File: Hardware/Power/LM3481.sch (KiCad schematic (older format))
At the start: 22 parts, among them IC1 LM3481MM, Q1 2N7000, Q2 AO4264E

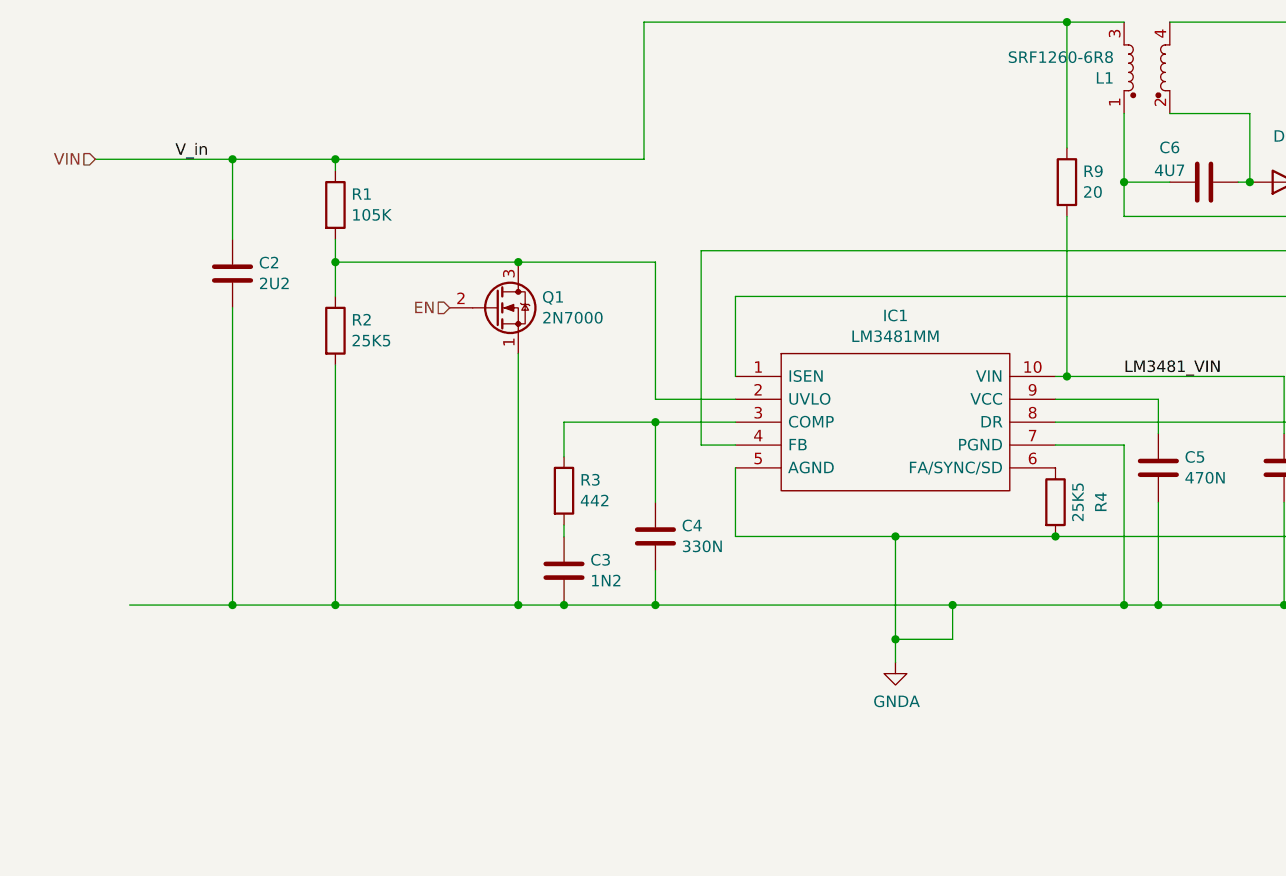
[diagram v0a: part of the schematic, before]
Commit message: Moved MCU Power Supply to Logic Board
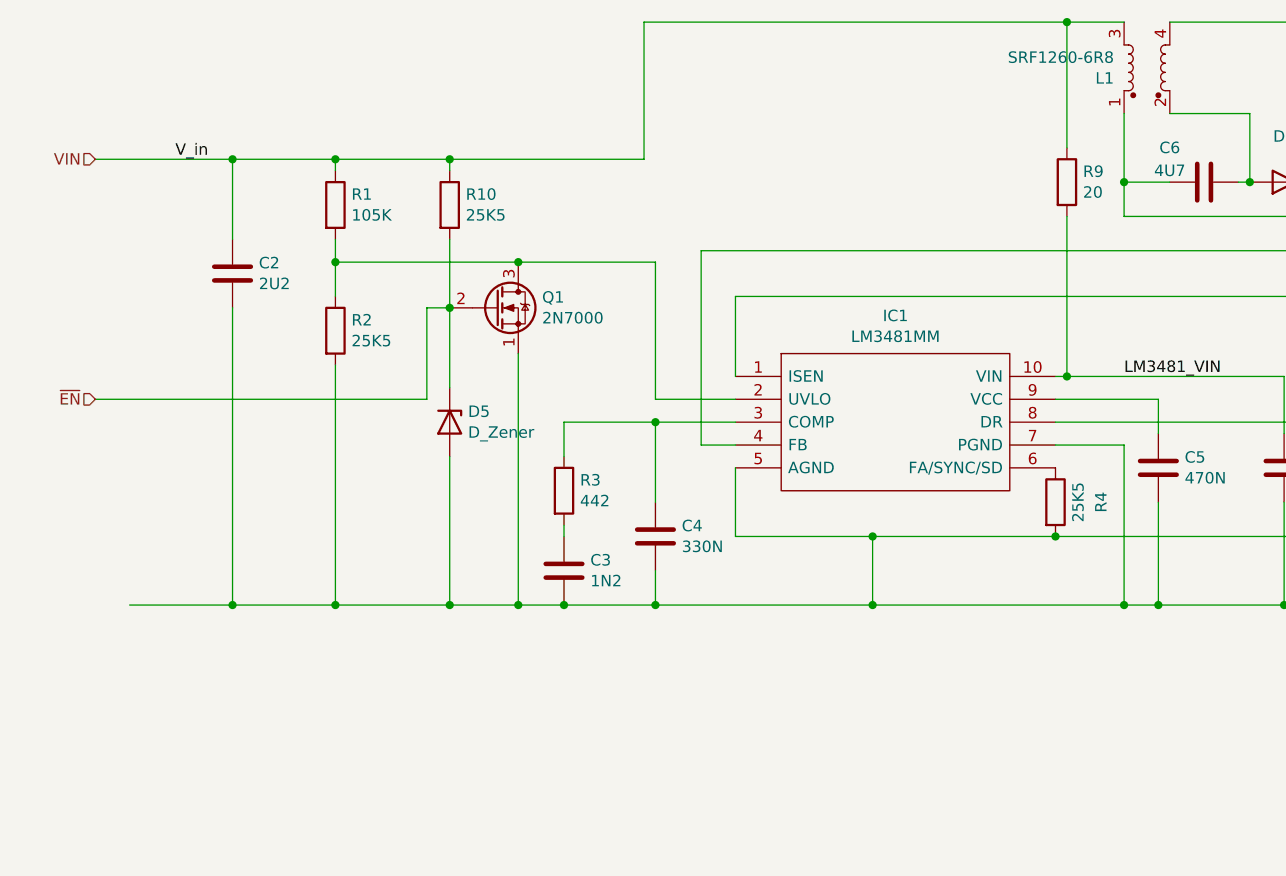
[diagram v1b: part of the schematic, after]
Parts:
- added D5: D_Zener, Diode_SMD:D_SOD-323_HandSoldering, symbol Device:D_Zener
- added R10: 25K5, Resistor_SMD:R_0603_1608Metric_Pad1.05x0.95mm_HandSolder, symbol Device:R
- D1: Arrow Part Number (none) -> C19229; Mouser Part Number C19229 -> (none)
- IC1: Manufacturer_Part_Number LM3481MM -> (none); Mouser Part Number (none) -> LM3481MM
- L1: Manufacturer_Part_Number SRF1260-6R8 -> (none); Mouser Part Number (none) -> SRF1260-6R8
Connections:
- net VIN: now also R10.1
- net EN renamed ~EN
- net ~EN: now also D5.1 (K), R10.2
- net GNDA renamed GNDPWR
- net GNDPWR: now also D5.2 (A)
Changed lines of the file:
@@
 F 2 "ArduinoLamp:D_SMC_Handsoldering_Shortened" H 7250 2900 50  0001 C CNN
 F 3 "~" H 7250 2900 50  0001 C CNN
-F 4 "C19229" H 7250 2900 50  0001 C CNN "Mouser Part Number"
+F 4 "" H 7250 2900 50  0001 C CNN "Mouser Part Number"
+F 5 "C19229" H 7250 2900 50  0001 C CNN "Arrow Part Number"
 	1    7250 2900
 	-1   0    0    1
@@
 F 2 "ArduinoLamp:L_Bourns_SRF1260_HandSoldering" H 6650 2400 50  0001 C CNN
 F 3 "~" H 6650 2400 50  0001 C CNN
-F 4 "SRF1260-6R8" H 6650 2400 50  0001 C CNN "Manufacturer_Part_Number"
+F 4 "" H 6650 2400 50  0001 C CNN "Manufacturer_Part_Number"
+F 5 "SRF1260-6R8" H 6650 2400 50  0001 C CNN "Mouser Part Number"
 	1    6650 2400
 	0    -1   -1   0
@@
 F 5 "1.1" H 6100 3550 50  0001 L CNN "Height"
 F 6 "Texas Instruments" H 6100 3450 50  0001 L CNN "Manufacturer_Name"
-F 7 "LM3481MM" H 6100 3350 50  0001 L CNN "Manufacturer_Part_Number"
+F 7 "" H 6100 3350 50  0001 L CNN "Manufacturer_Part_Number"
 F 8 "" H 6100 3250 50  0001 L CNN "Arrow Part Number"
 F 9 "" H 6100 3150 50  0001 L CNN "Arrow Price/Stock"
-F 10 "" H 6100 3050 50  0001 L CNN "Mouser Part Number"
+F 10 "LM3481MM" H 6100 3050 50  0001 L CNN "Mouser Part Number"
 F 11 "" H 6100 2950 50  0001 L CNN "Mouser Price/Stock"
 	1    4850 3750
@@
 V_in
 Wire Wire Line
-	3100 2800 4450 2800
+	3100 2800 3600 2800
+Text HLabel 2050 2800 0    50   Input ~ 0
+VIN
+Text HLabel 10150 3350 2    50   Input ~ 0
+VOUT
+Connection ~ 4100 4750
+Wire Wire Line
+	4100 4750 3900 4750
+Wire Wire Line
+	4100 4750 4500 4750
+Wire Wire Line
+	4500 4300 4500 3950
+Connection ~ 4500 3950
+Wire Wire Line
+	4500 3950 4850 3950
+Wire Wire Line
+	4500 4600 4500 4750
+Connection ~ 4500 4750
+Wire Wire Line
+	4100 4100 4100 3950
+Wire Wire Line
+	4100 3950 4500 3950
+Wire Wire Line
+	4100 4400 4100 4450
+Text Notes 7350 7500 0    50   ~ 0
+LM3481 SEPIC Converter
+Connection ~ 3900 4750
+Wire Wire Line
+	3900 3650 3900 4750
+Wire Wire Line
+	2200 4750 2650 4750
+Connection ~ 2650 4750
+Wire Wire Line
+	2650 4750 3100 4750
+Connection ~ 3100 4750
+Wire Wire Line
+	3100 4750 3600 4750
+Wire Wire Line
+	6750 2200 8800 2200
+Wire Wire Line
+	8800 2200 8800 4750
+Connection ~ 8800 4750
+Wire Wire Line
+	8800 4750 9150 4750
+Wire Wire Line
+	9600 3350 10150 3350
+Wire Wire Line
+	2050 2800 2650 2800
+Text Label 6550 3750 0    50   ~ 0
+LM3481_VIN
+Connection ~ 7250 4750
+Wire Wire Line
+	6250 4050 6550 4050
+Wire Wire Line
+	6550 4050 6550 4750
+Connection ~ 6550 4750
+Wire Wire Line
+	6550 4750 6700 4750
+Wire Wire Line
+	6700 4300 6700 4750
+Connection ~ 6700 4750
+Wire Wire Line
+	6700 4750 7250 4750
+Wire Wire Line
+	4850 4150 4850 4450
+Wire Wire Line
+	7750 4750 8400 4750
+Wire Wire Line
+	8400 4000 8400 4050
+Connection ~ 8400 4000
+Wire Wire Line
+	8400 4350 8400 4750
+Connection ~ 8400 4750
+Wire Wire Line
+	8400 4750 8800 4750
+Wire Wire Line
+	6250 4450 9150 4450
+Wire Wire Line
+	9150 4450 9150 4150
+Connection ~ 6250 4450
+Wire Wire Line
+	4450 2200 6300 2200
+$Comp
+L Device:R R9
+U 1 1 5FA1346B
+P 6300 2900
+F 0 "R9" H 6370 2946 50  0000 L CNN
+F 1 "20" H 6370 2855 50  0000 L CNN
+F 2 "Resistor_SMD:R_0603_1608Metric_Pad1.05x0.95mm_HandSolder" V 6230 2900 50  0001 C CNN
+F 3 "~" H 6300 2900 50  0001 C CNN
+F 4 "RS-03K19R6FT" H 6300 2900 50  0001 C CNN "Manufacturer_Part_Number"
+	1    6300 2900
+	1    0    0    -1
+$EndComp
+Wire Wire Line
+	6300 2750 6300 2200
+Connection ~ 6300 2200
+Wire Wire Line
+	6300 2200 6550 2200
+Wire Wire Line
+	6300 3050 6300 3750
+Wire Wire Line
+	6250 3750 6300 3750
+Connection ~ 6300 3750
+Wire Wire Line
+	6300 3750 7250 3750
+Wire Wire Line
+	4850 4450 5450 4450
+Wire Wire Line
+	4500 4750 5450 4750
+Wire Wire Line
+	3900 3250 4500 3250
+Connection ~ 3900 3250
 Wire Wire Line
 	3100 3250 3900 3250
@@
 	1    0    0    -1
 $EndComp
-Connection ~ 3900 3250
-Wire Wire Line
-	3900 3250 4500 3250
-Text HLabel 2050 2800 0    50   Input ~ 0
-VIN
-Text HLabel 3600 3450 0    50   Input ~ 0
-EN
-Text HLabel 10150 3350 2    50   Input ~ 0
-VOUT
-Connection ~ 4100 4750
-Wire Wire Line
-	4100 4750 3900 4750
-Wire Wire Line
-	4100 4750 4500 4750
-Wire Wire Line
-	4500 4300 4500 3950
-Connection ~ 4500 3950
-Wire Wire Line
-	4500 3950 4850 3950
-Wire Wire Line
-	4500 4600 4500 4750
-Connection ~ 4500 4750
-Wire Wire Line
-	4100 4100 4100 3950
-Wire Wire Line
-	4100 3950 4500 3950
-Wire Wire Line
-	4100 4400 4100 4450
-Text Notes 7350 7500 0    50   ~ 0
-LM3481 SEPIC Converter
-Connection ~ 3900 4750
-Wire Wire Line
-	3900 3650 3900 4750
-Wire Wire Line
-	2200 4750 2650 4750
-Connection ~ 2650 4750
-Wire Wire Line
-	2650 4750 3100 4750
-Connection ~ 3100 4750
-Wire Wire Line
-	3100 4750 3900 4750
-Wire Wire Line
-	6750 2200 8800 2200
-Wire Wire Line
-	8800 2200 8800 4750
-Connection ~ 8800 4750
-Wire Wire Line
-	8800 4750 9150 4750
-Wire Wire Line
-	9600 3350 10150 3350
-Wire Wire Line
-	2050 2800 2650 2800
-Text Label 6550 3750 0    50   ~ 0
-LM3481_VIN
-$Comp
-L power:GNDA #PWR0113
-U 1 1 5F9A8242
-P 5550 5000
-F 0 "#PWR0113" H 5550 4750 50  0001 C CNN
-F 1 "GNDA" H 5555 4827 50  0000 C CNN
-F 2 "" H 5550 5000 50  0001 C CNN
-F 3 "" H 5550 5000 50  0001 C CNN
-	1    5550 5000
-	1    0    0    -1
-$EndComp
-Connection ~ 7250 4750
-Wire Wire Line
-	6250 4050 6550 4050
-Wire Wire Line
-	6550 4050 6550 4750
-Connection ~ 6550 4750
-Wire Wire Line
-	6550 4750 6700 4750
-Wire Wire Line
-	6700 4300 6700 4750
-Connection ~ 6700 4750
-Wire Wire Line
-	6700 4750 7250 4750
-Wire Wire Line
-	4500 4750 5800 4750
-Wire Wire Line
-	4850 4150 4850 4450
-Wire Wire Line
-	4850 4450 5550 4450
-Wire Wire Line
-	5550 4450 5550 4900
-Connection ~ 5550 4450
-Wire Wire Line
-	5550 4450 6250 4450
-Wire Wire Line
-	7750 4750 8400 4750
-Wire Wire Line
-	8400 4000 8400 4050
-Connection ~ 8400 4000
-Wire Wire Line
-	8400 4350 8400 4750
-Connection ~ 8400 4750
-Wire Wire Line
-	8400 4750 8800 4750
-Wire Wire Line
-	6250 4450 9150 4450
-Wire Wire Line
-	9150 4450 9150 4150
-Connection ~ 6250 4450
-Wire Wire Line
-	5550 4900 5800 4900
-Wire Wire Line
-	5800 4900 5800 4750
-Connection ~ 5550 4900
-Wire Wire Line
-	5550 4900 5550 5000
-Connection ~ 5800 4750
-Wire Wire Line
-	5800 4750 6550 4750
-Wire Wire Line
-	4450 2200 6300 2200
-$Comp
-L Device:R R9
-U 1 1 5FA1346B
-P 6300 2900
-F 0 "R9" H 6370 2946 50  0000 L CNN
-F 1 "20" H 6370 2855 50  0000 L CNN
-F 2 "Resistor_SMD:R_0603_1608Metric_Pad1.05x0.95mm_HandSolder" V 6230 2900 50  0001 C CNN
-F 3 "~" H 6300 2900 50  0001 C CNN
-F 4 "RS-03K19R6FT" H 6300 2900 50  0001 C CNN "Manufacturer_Part_Number"
-	1    6300 2900
-	1    0    0    -1
-$EndComp
-Wire Wire Line
-	6300 2750 6300 2200
-Connection ~ 6300 2200
-Wire Wire Line
-	6300 2200 6550 2200
-Wire Wire Line
-	6300 3050 6300 3750
-Wire Wire Line
-	6250 3750 6300 3750
-Connection ~ 6300 3750
-Wire Wire Line
-	6300 3750 7250 3750
+$Comp
+L Device:R R10
+U 1 1 5FBCFFB7
+P 3600 3000
+F 0 "R10" H 3670 3046 50  0000 L CNN
+F 1 "25K5" H 3670 2955 50  0000 L CNN
+F 2 "Resistor_SMD:R_0603_1608Metric_Pad1.05x0.95mm_HandSolder" V 3530 3000 50  0001 C CNN
+F 3 "~" H 3600 3000 50  0001 C CNN
+F 4 "RS-05K2552FT" H 3600 3000 50  0001 C CNN "Manufacturer_Part_Number"
+	1    3600 3000
+	1    0    0    -1
+$EndComp
+Wire Wire Line
+	3600 2850 3600 2800
+Connection ~ 3600 2800
+Wire Wire Line
+	3600 2800 4450 2800
+Wire Wire Line
+	3600 3150 3600 3450
+$Comp
+L Device:D_Zener D5
+U 1 1 5FBD5B24
+P 3600 3950
+F 0 "D5" V 3554 4030 50  0000 L CNN
+F 1 "D_Zener" V 3645 4030 50  0000 L CNN
+F 2 "Diode_SMD:D_SOD-323_HandSoldering" H 3600 3950 50  0001 C CNN
+F 3 "~" H 3600 3950 50  0001 C CNN
+F 4 "MM3Z4V7ST1G" H 3600 3950 50  0001 C CNN "Mouser Part Number"
+	1    3600 3950
+	0    1    1    0
+$EndComp
+Wire Wire Line
+	3600 3450 3600 3800
+Connection ~ 3600 3450
+Wire Wire Line
+	3600 4100 3600 4750
+Connection ~ 3600 4750
+Wire Wire Line
+	3600 4750 3900 4750
+Text HLabel 2050 3850 0    50   Input ~ 0
+~EN
+Wire Wire Line
+	2050 3850 3500 3850
+Wire Wire Line
+	3500 3850 3500 3450
+Wire Wire Line
+	3500 3450 3600 3450
+Wire Wire Line
+	5450 4450 5450 4750
+Connection ~ 5450 4450
+Wire Wire Line
+	5450 4450 6250 4450
+Connection ~ 5450 4750
+Wire Wire Line
+	5450 4750 6550 4750
 $EndSCHEMATC

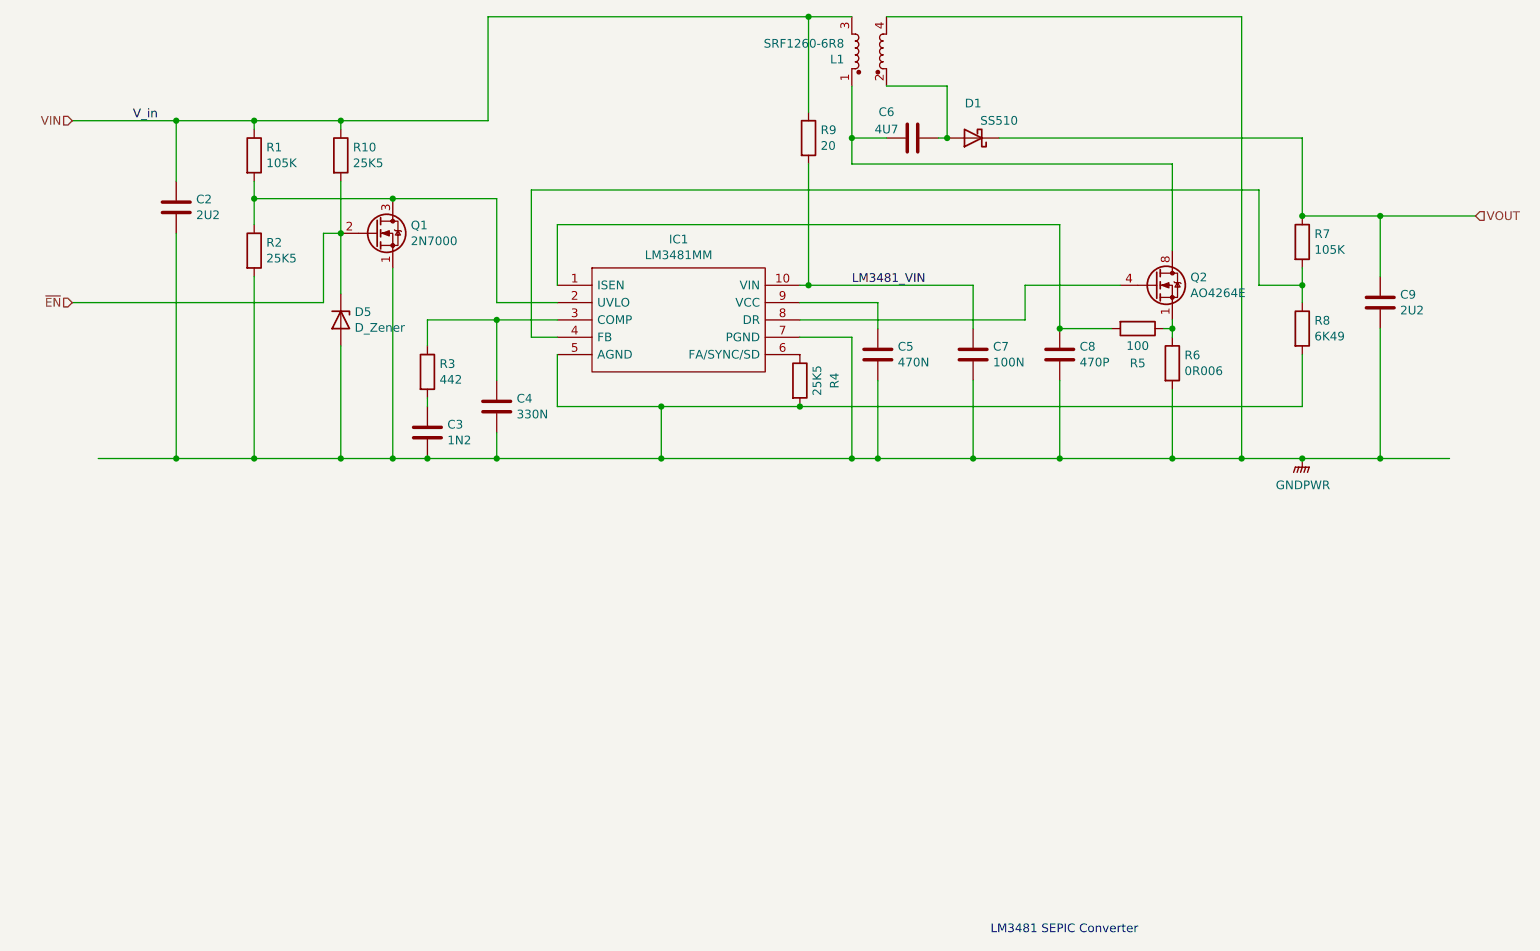
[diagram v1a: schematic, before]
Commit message: Removed Logic Board PSU from Power Board
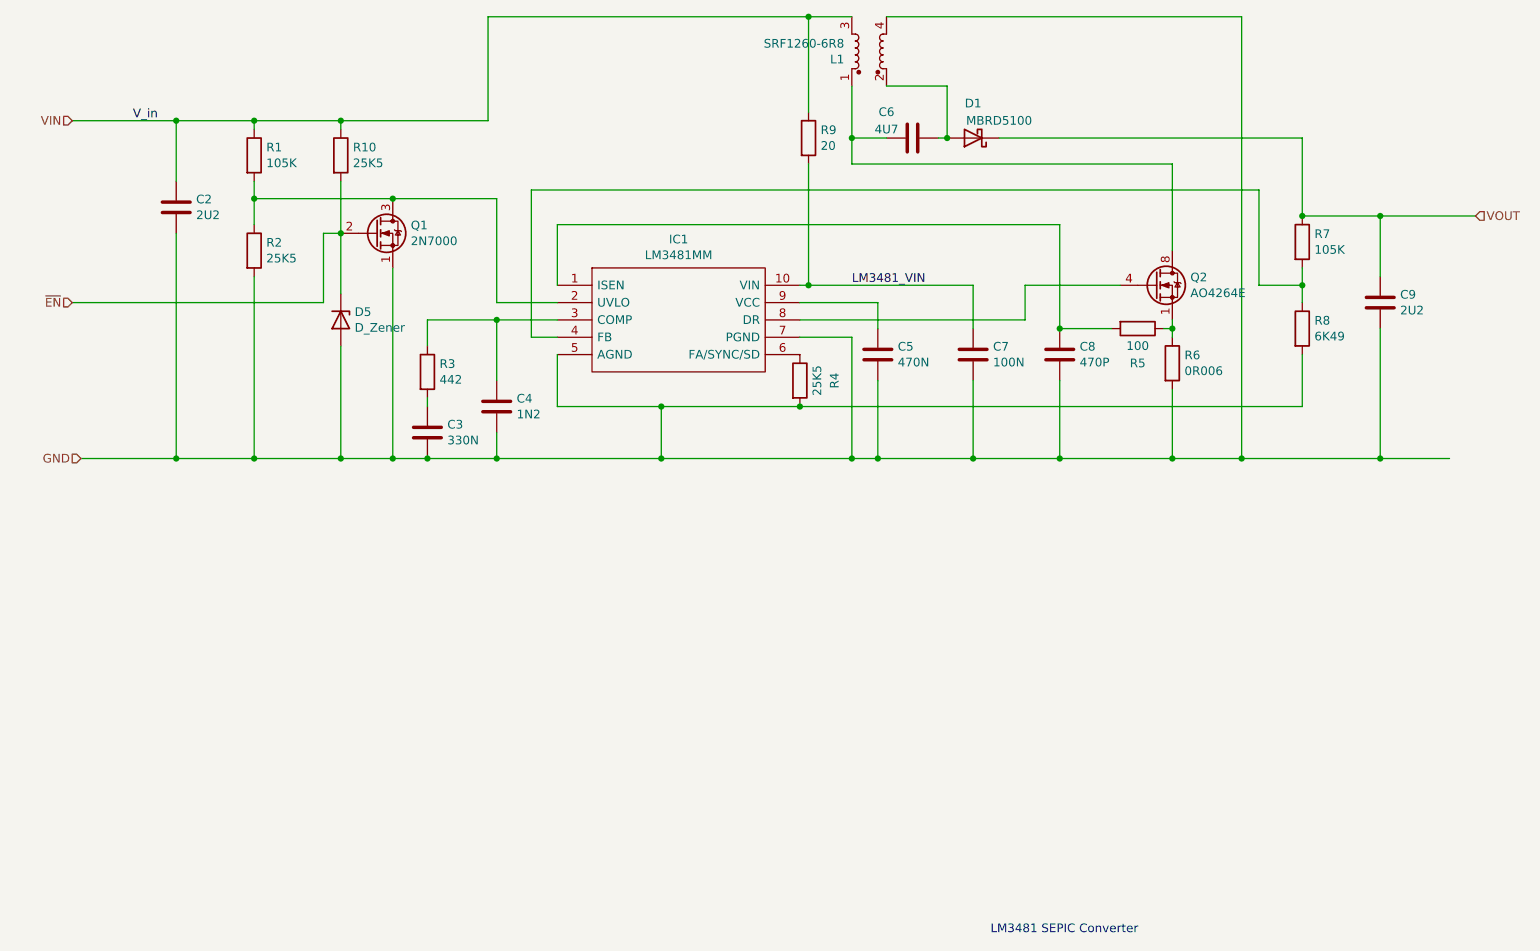
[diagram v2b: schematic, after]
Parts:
- C3: value 1N2 -> 330N; Manufacturer_Part_Number C1608C0G1H122JT000N -> TCC0603X7R334K500CT
- C4: value 330N -> 1N2; Manufacturer_Part_Number TCC0603X7R334K500CT -> C1608C0G1H122JT000N
- D1: value SS510 -> MBRD5100; footprint ArduinoLamp:D_SMC_Handsoldering_Shortened -> ArduinoLamp:TO-252-2_ConnectedPins
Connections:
- net GNDPWR renamed GND
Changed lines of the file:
@@
-	1    0    0    -1
-$EndComp
-$Comp
-L power:GNDPWR #PWR0101
-U 1 1 5F852F9B
-P 9150 4750
-F 0 "#PWR0101" H 9150 4550 50  0001 C CNN
-F 1 "GNDPWR" H 9154 4596 50  0000 C CNN
-F 2 "" H 9150 4700 50  0001 C CNN
-F 3 "" H 9150 4700 50  0001 C CNN
-	1    9150 4750
 	1    0    0    -1
 $EndComp
@@
 Connection ~ 9600 3350
 Wire Wire Line
-	9600 4750 9150 4750
-Connection ~ 9150 4750
-Wire Wire Line
 	9600 4750 10000 4750
 Connection ~ 9600 4750
@@
 P 7250 2900
 F 0 "D1" H 7250 2700 50  0000 C CNN
-F 1 "SS510" H 7100 2800 50  0000 C CNN
-F 2 "ArduinoLamp:D_SMC_Handsoldering_Shortened" H 7250 2900 50  0001 C CNN
+F 1 "MBRD5100" H 7100 2800 50  0000 C CNN
+F 2 "ArduinoLamp:TO-252-2_ConnectedPins" H 7250 2900 50  0001 C CNN
 F 3 "~" H 7250 2900 50  0001 C CNN
 F 4 "" H 7250 2900 50  0001 C CNN "Mouser Part Number"
@@
 P 4100 4600
 F 0 "C3" H 4215 4646 50  0000 L CNN
-F 1 "1N2" H 4215 4555 50  0000 L CNN
+F 1 "330N" H 4215 4555 50  0000 L CNN
 F 2 "Capacitor_SMD:C_0603_1608Metric_Pad1.05x0.95mm_HandSolder" H 4138 4450 50  0001 C CNN
 F 3 "~" H 4100 4600 50  0001 C CNN
-F 4 "C1608C0G1H122JT000N" H 4100 4600 50  0001 C CNN "Manufacturer_Part_Number"
+F 4 "TCC0603X7R334K500CT" H 4100 4600 50  0001 C CNN "Manufacturer_Part_Number"
 	1    4100 4600
 	1    0    0    -1
@@
 P 4500 4450
 F 0 "C4" H 4615 4496 50  0000 L CNN
-F 1 "330N" H 4615 4405 50  0000 L CNN
+F 1 "1N2" H 4615 4405 50  0000 L CNN
 F 2 "Capacitor_SMD:C_0603_1608Metric_Pad1.05x0.95mm_HandSolder" H 4538 4300 50  0001 C CNN
 F 3 "~" H 4500 4450 50  0001 C CNN
-F 4 "TCC0603X7R334K500CT" H 4500 4450 50  0001 C CNN "Manufacturer_Part_Number"
+F 4 "C1608C0G1H122JT000N" H 4500 4450 50  0001 C CNN "Manufacturer_Part_Number"
 	1    4500 4450
 	1    0    0    -1
@@
 Wire Wire Line
 	3900 3650 3900 4750
-Wire Wire Line
-	2200 4750 2650 4750
 Connection ~ 2650 4750
 Wire Wire Line
@@
 	8800 2200 8800 4750
 Connection ~ 8800 4750
-Wire Wire Line
-	8800 4750 9150 4750
 Wire Wire Line
 	9600 3350 10150 3350
@@
 Wire Wire Line
 	5450 4750 6550 4750
+Wire Wire Line
+	8800 4750 9600 4750
+Text HLabel 2100 4750 0    50   Input ~ 0
+GND
+Wire Wire Line
+	2100 4750 2650 4750
 $EndSCHEMATC
